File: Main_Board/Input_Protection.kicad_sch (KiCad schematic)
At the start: 11 parts, among them IC1 TPS25200DRVR, U6 SS351AT

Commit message: Fix schematic readibility
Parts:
- R34: value 39k -> 39K
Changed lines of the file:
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@@
 	(text "Policzyć Rilm gdy będzie wiadomy docelowy pobór!"
 		(exclude_from_sim no)
-		(at 143.002 124.968 0)
+		(at 143.764 128.778 0)
 		(effects
 			(font
@@
 			)
 		)
-		(property "Value" "39k"
-			(at 164.338 105.156 0)
-			(show_name no)
-			(do_not_autoplace no)
+		(property "Value" "39K"
+			(at 164.846 105.156 0)
+			(show_name no)
+			(do_not_autoplace no)

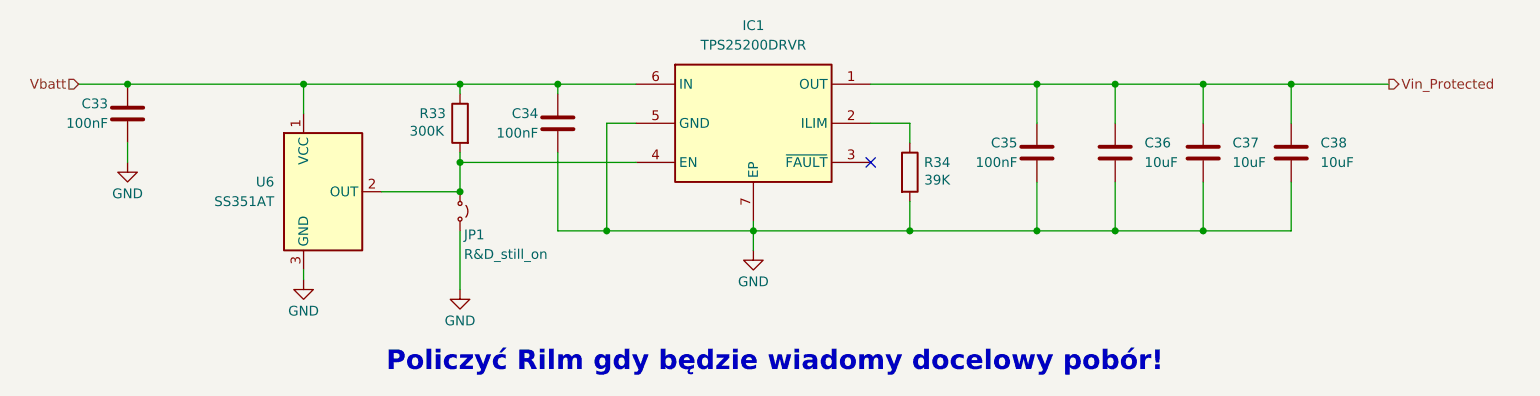
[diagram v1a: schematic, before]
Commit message: Standardise resistor value mark for BOM + pyro footprints
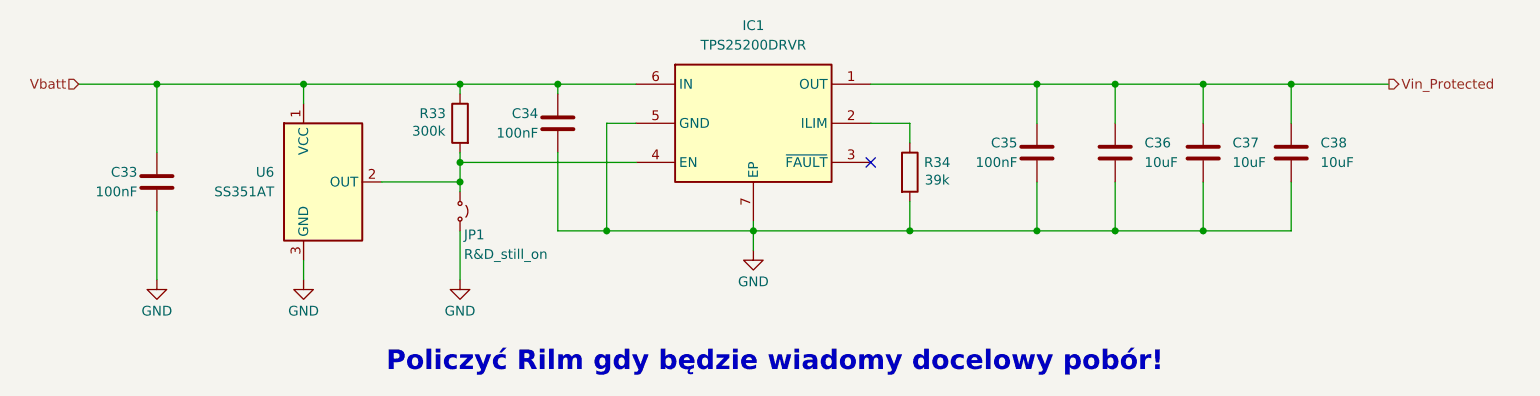
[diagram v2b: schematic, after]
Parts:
- R33: value 300K -> 300k
- R34: value 39K -> 39k
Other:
- moved on the sheet: C33, U6
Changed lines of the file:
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@@
 	)
 	(junction
-		(at 102.87 106.68)
+		(at 82.55 92.71)
 		(diameter 0)
 		(color 0 0 0 0)
@@
 	)
 	(junction
-		(at 59.69 92.71)
+		(at 63.5 92.71)
 		(diameter 0)
 		(color 0 0 0 0)
@@
 	)
 	(junction
-		(at 82.55 92.71)
-		(diameter 0)
-		(color 0 0 0 0)
-	)
-	(junction
 		(at 177.8 92.71)
 		(diameter 0)
@@
 	)
 	(junction
+		(at 102.87 105.41)
+		(diameter 0)
+		(color 0 0 0 0)
+	)
+	(junction
 		(at 140.97 111.76)
 		(diameter 0)
@@
 	(wire
 		(pts
-			(xy 53.34 92.71) (xy 59.69 92.71)
+			(xy 53.34 92.71) (xy 63.5 92.71)
 		)
 		(stroke
@@
 	(wire
 		(pts
-			(xy 59.69 100.33) (xy 59.69 102.87)
+			(xy 63.5 109.22) (xy 63.5 118.11)
 		)
 		(stroke
@@
 	(wire
 		(pts
-			(xy 82.55 96.52) (xy 82.55 92.71)
+			(xy 82.55 95.25) (xy 82.55 92.71)
 		)
 		(stroke
@@
 	(wire
 		(pts
-			(xy 102.87 119.38) (xy 102.87 111.76)
+			(xy 102.87 118.11) (xy 102.87 111.76)
 		)
 		(stroke
@@
 	(wire
 		(pts
-			(xy 92.71 106.68) (xy 102.87 106.68)
+			(xy 63.5 101.6) (xy 63.5 92.71)
+		)
+		(stroke
+			(width 0)
+			(type default)
+		)
+	)
+	(wire
+		(pts
+			(xy 92.71 105.41) (xy 102.87 105.41)
 		)
 		(stroke
@@
 	(wire
 		(pts
-			(xy 82.55 118.11) (xy 82.55 116.84)
+			(xy 82.55 118.11) (xy 82.55 115.57)
 		)
 		(stroke
@@
 	(wire
 		(pts
+			(xy 63.5 92.71) (xy 82.55 92.71)
+		)
+		(stroke
+			(width 0)
+			(type default)
+		)
+	)
+	(wire
+		(pts
 			(xy 115.57 101.6) (xy 115.57 111.76)
 		)
@@
 	(wire
 		(pts
-			(xy 102.87 106.68) (xy 102.87 102.87)
+			(xy 102.87 106.68) (xy 102.87 105.41)
 		)
 		(stroke
@@
 	(wire
 		(pts
+			(xy 102.87 105.41) (xy 102.87 102.87)
+		)
+		(stroke
+			(width 0)
+			(type default)
+		)
+	)
+	(wire
+		(pts
 			(xy 125.73 92.71) (xy 115.57 92.71)
-		)
-		(stroke
-			(width 0)
-			(type default)
-		)
-	)
-	(wire
-		(pts
-			(xy 59.69 92.71) (xy 82.55 92.71)
 		)
 		(stroke
@@
 			)
 		)
-		(property "Value" "300K"
-			(at 98.552 98.806 0)
+		(property "Value" "300k"
+			(at 98.806 98.806 0)
 			(show_name no)
 			(do_not_autoplace no)
@@
 	(symbol
 		(lib_id "Sensor_Magnetic:DRV5033AJxDBZ")
-		(at 85.09 106.68 0)
+		(at 85.09 105.41 0)
 		(unit 1)
 		(body_style 1)
@@
 		(fields_autoplaced yes)
 		(property "Reference" "U6"
-			(at 78.74 105.4099 0)
+			(at 78.74 104.1399 0)
 			(show_name no)
 			(do_not_autoplace no)
@@
 		)
 		(property "Value" "SS351AT"
-			(at 78.74 107.9499 0)
+			(at 78.74 106.6799 0)
 			(show_name no)
 			(do_not_autoplace no)
@@
 		)
 		(property "Footprint" "Package_TO_SOT_SMD:SOT-23"
-			(at 85.09 106.68 0)
+			(at 85.09 105.41 0)
 			(hide yes)
 			(show_name no)
@@
 		)
 		(property "Datasheet" "https://www.ti.com/lit/ds/symlink/drv5033.pdf"
-			(at 85.09 106.68 0)
+			(at 85.09 105.41 0)
 			(hide yes)
 			(show_name no)
@@
 		)
 		(property "Description" "±6.9 / ±3.5 mT, 20-kHz, 2-38V, SOT-23"
-			(at 85.09 106.68 0)
+			(at 85.09 105.41 0)
 			(hide yes)
 			(show_name no)
@@
 	(symbol
 		(lib_id "power:GND")
-		(at 59.69 102.87 0)
+		(at 63.5 118.11 0)
 		(unit 1)
 		(body_style 1)
@@
 		(dnp no)
 		(property "Reference" "#PWR087"
-			(at 59.69 109.22 0)
+			(at 63.5 124.46 0)
 			(hide yes)
 			(show_name no)
@@
 		)
 		(property "Value" "GND"
-			(at 59.69 106.934 0)
+			(at 63.5 122.174 0)
 			(show_name no)
 			(do_not_autoplace no)
@@
 		)
 		(property "Footprint" ""
-			(at 59.69 102.87 0)
+			(at 63.5 118.11 0)
 			(hide yes)
 			(show_name no)
@@
 		)
 		(property "Datasheet" ""
-			(at 59.69 102.87 0)
+			(at 63.5 118.11 0)
 			(hide yes)
 			(show_name no)
@@
 		)
 		(property "Description" "Power symbol creates a global label with name \"GND\" , ground"
-			(at 59.69 102.87 0)
+			(at 63.5 118.11 0)
 			(hide yes)
 			(show_name no)
@@
 	(symbol
 		(lib_id "Device:C")
-		(at 59.69 96.52 0)
+		(at 63.5 105.41 0)
 		(mirror y)
 		(unit 1)
@@
 		(dnp no)
 		(property "Reference" "C33"
-			(at 57.15 95.25 0)
+			(at 60.96 104.14 0)
 			(show_name no)
 			(do_not_autoplace no)
@@
 		)
 		(property "Value" "100nF"
-			(at 57.15 97.79 0)
+			(at 60.96 106.68 0)
 			(show_name no)
 			(do_not_autoplace no)
@@
 		)
 		(property "Footprint" "Capacitor_SMD:C_0603_1608Metric"
-			(at 58.7248 100.33 0)
+			(at 62.5348 109.22 0)
 			(hide yes)
 			(show_name no)
@@
 		)
 		(property "Datasheet" ""
-			(at 59.69 96.52 0)
+			(at 63.5 105.41 0)
 			(hide yes)
 			(show_name no)
@@
 		)
 		(property "Description" "Unpolarized capacitor"
-			(at 59.69 96.52 0)
+			(at 63.5 105.41 0)
 			(hide yes)
 			(show_name no)
@@
 			)
 		)
-		(property "Value" "39K"
+		(property "Value" "39k"
 			(at 164.846 105.156 0)
 			(show_name no)
@@
 	(symbol
 		(lib_id "power:GND")
-		(at 102.87 119.38 0)
+		(at 102.87 118.11 0)
 		(unit 1)
 		(body_style 1)
@@
 		(dnp no)
 		(property "Reference" "#PWR089"
-			(at 102.87 125.73 0)
+			(at 102.87 124.46 0)
 			(hide yes)
 			(show_name no)
@@
 		)
 		(property "Value" "GND"
-			(at 102.87 123.444 0)
+			(at 102.87 122.174 0)
 			(show_name no)
 			(do_not_autoplace no)
@@
 		)
 		(property "Footprint" ""
-			(at 102.87 119.38 0)
+			(at 102.87 118.11 0)
 			(hide yes)
 			(show_name no)
@@
 		)
 		(property "Datasheet" ""
-			(at 102.87 119.38 0)
+			(at 102.87 118.11 0)
 			(hide yes)
 			(show_name no)
@@
 		)
 		(property "Description" "Power symbol creates a global label with name \"GND\" , ground"
-			(at 102.87 119.38 0)
-			(hide yes)
-			(show_name no)
+			(at 102.87 118.11 0)
+			(hide yes)
+			(show_name no)

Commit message: fix shema after review
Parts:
- R33: value 300k -> 10k
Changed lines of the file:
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@@
 			)
 		)
-		(property "Value" "300k"
+		(property "Value" "10k"
 			(at 98.806 98.806 0)
 			(show_name no)
